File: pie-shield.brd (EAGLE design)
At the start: 160 x 100 mm, 20 parts, among them IC4 NRF24L01SMD, Q2 3.2X2.5CRYSTAL

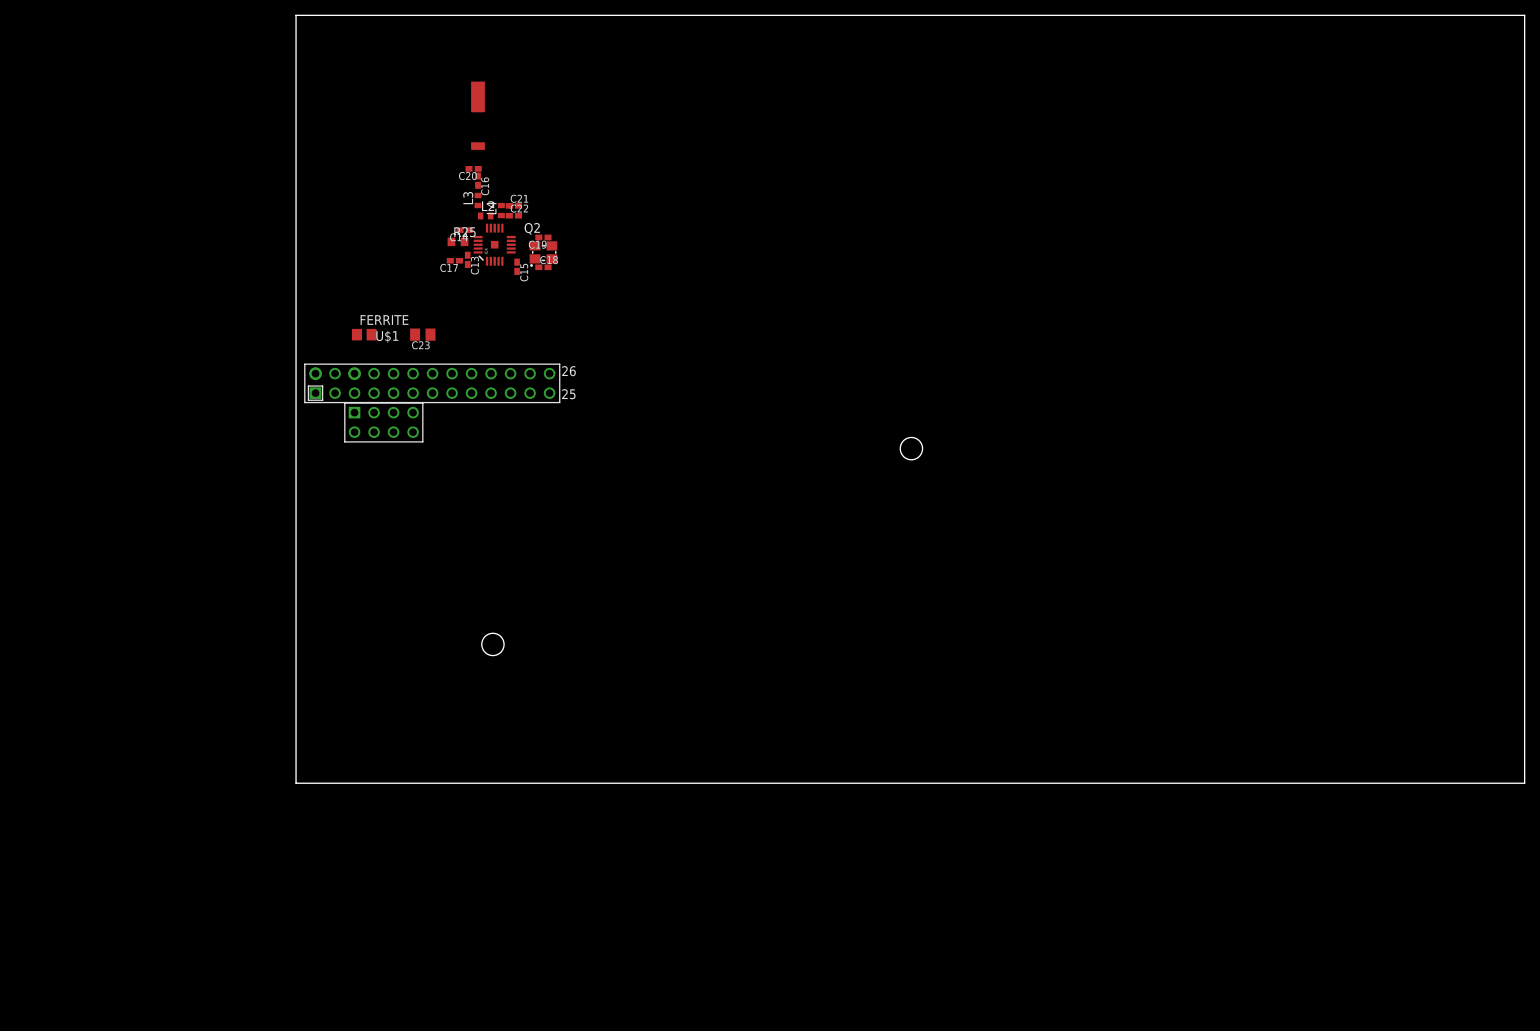
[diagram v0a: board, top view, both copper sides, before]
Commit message: sized board down
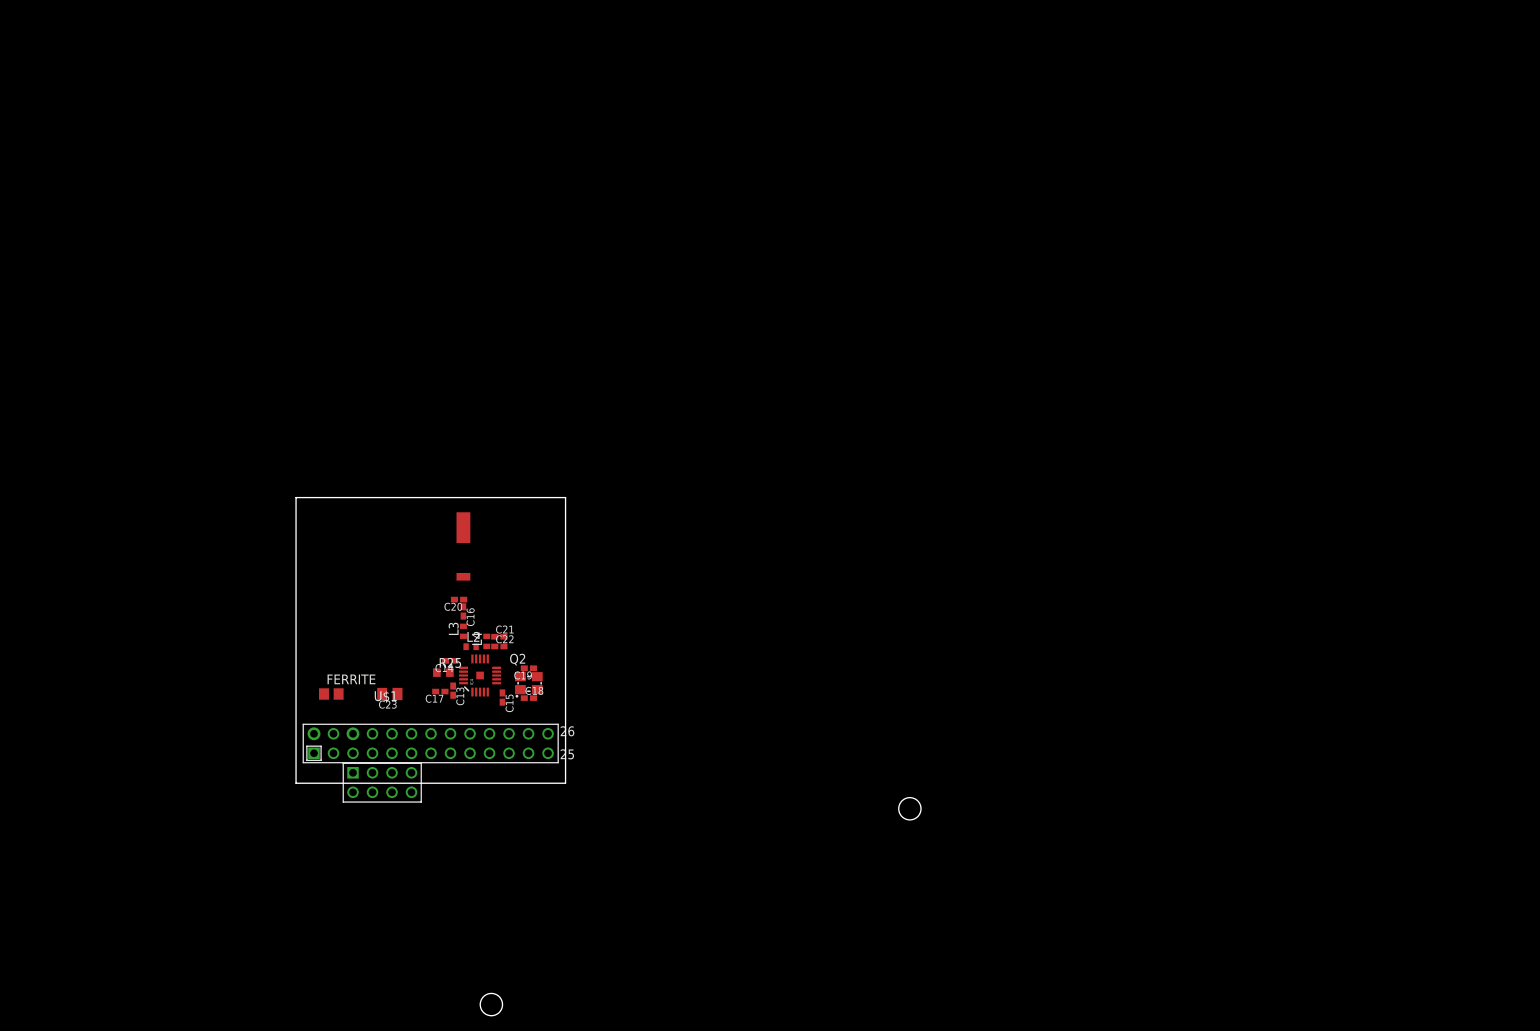
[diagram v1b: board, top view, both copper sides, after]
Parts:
- moved ANT 56.1 mm to (21.8, 29.3)
- moved C15 56.1 mm to (26.9, 11.2)
- moved C17 56.1 mm to (18.8, 11.9)
- moved C20 56.1 mm to (21.2, 23.9)
- moved C21 56.1 mm to (26.5, 19.1)
- moved C14 56.1 mm to (20.1, 15.9)
- moved L3 56.1 mm to (21.8, 19.8)
- moved R25 56.1 mm to (19.2, 14.4)
- moved C13 56.1 mm to (20.5, 12.1)
- moved C16 56.1 mm to (21.8, 22.4)
- moved C18 56.1 mm to (30.3, 11.1)
- moved C19 56.1 mm to (30.3, 15.0)
- moved C22 56.1 mm to (26.5, 17.8)
- moved IC4 56.1 mm to (24.0, 14.0)
- moved L2 56.1 mm to (22.8, 17.8)
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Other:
- board size 160 x 100 mm -> 35.1 x 37.2 mm

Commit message: minisized
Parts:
- moved ANT 15.1 mm to (10.2, 19.7)
- moved C18 13.7 mm to (26.0, 24.1), turned to 90 degrees
- moved Q2 12.7 mm to (24.1, 24.1), turned to 90 degrees
- moved C19 12.3 mm to (22.1, 24.1), turned to 90 degrees
- moved C20 11.3 mm to (12.6, 16.6), turned to 270 degrees
- moved C15 10.1 mm to (25.8, 21.2), turned to 0 degrees
- moved C21 9.47 mm to (17.4, 21.9), turned to 90 degrees
- moved C16 9.23 mm to (14.1, 17.2), turned to 0 degrees
- moved C22 8.78 mm to (18.7, 21.9), turned to 90 degrees
- moved C17 7.99 mm to (26.1, 15.1), turned to 0 degrees
- moved L4 7.03 mm to (18.0, 20.2), turned to 180 degrees
- moved L3 5.69 mm to (16.7, 17.2), turned to 180 degrees
- moved L2 4.09 mm to (18.7, 18.2), turned to 90 degrees
- moved IC4 3.83 mm to (23.1, 17.8), turned to 180 degrees
- moved C13 3.62 mm to (23.8, 13.4)
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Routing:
- net +3V3_RF: track 0.00 -> 47.4 mm, vias 0 -> 3
- net +3V3: track 0.00 -> 7.04 mm
- net N$73: track 0.00 -> 6.46 mm
- net GND: track 0.00 -> 6.17 mm
- net N$11: track 0.00 -> 5.78 mm
- net N$10: track 0.00 -> 4.07 mm
- net N$78: track 0.00 -> 3.84 mm
- net N$79: track 0.00 -> 3.77 mm
- net N$12: track 0.00 -> 3.36 mm
- net N$70: track 0.00 -> 2.82 mm
- net N$71: track 0.00 -> 1.86 mm
- net N$80: track 0.00 -> 1.33 mm
- added copper zone on layer 1, net GND
- added copper zone on layer 16, net GND
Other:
- board size 35.1 x 37.2 mm -> 35.1 x 25.2 mm

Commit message: wired board
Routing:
- net N$10: track 4.07 -> 5.64 mm
- net +3V3_RF: track 47.4 -> 48.4 mm
- net GND: vias 0 -> 43
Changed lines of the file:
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@@
 <contactref element="U$1" pad="P1_9"/>
 <polygon width="0.3048" layer="1" orphans="yes" thermals="no">
-<vertex x="-0.4572" y="13.97"/>
-<vertex x="17.4498" y="14.0208"/>
+<vertex x="-0.7112" y="13.0302"/>
+<vertex x="12.319" y="13.0302"/>
+<vertex x="12.2936" y="15.8496"/>
 <vertex x="21.2852" y="15.6972"/>
-<vertex x="21.3868" y="20.574"/>
-<vertex x="21.336" y="27.7876"/>
+<vertex x="21.3614" y="20.701"/>
+<vertex x="19.5326" y="22.606"/>
+<vertex x="16.0274" y="22.5806"/>
+<vertex x="16.0528" y="27.178"/>
 <vertex x="36.0934" y="27.2034"/>
-<vertex x="35.941" y="-0.9906"/>
-<vertex x="-0.4572" y="-0.3302"/>
+<vertex x="35.7632" y="0.7366"/>
+<vertex x="-0.4064" y="1.016"/>
 </polygon>
 <polygon width="0.3048" layer="16">
-<vertex x="17.3228" y="13.8684"/>
+<vertex x="-0.7112" y="12.954"/>
+<vertex x="12.2936" y="12.954"/>
+<vertex x="12.3444" y="15.9004"/>
 <vertex x="21.2344" y="15.748"/>
-<vertex x="21.2598" y="28.0416"/>
+<vertex x="21.3614" y="20.7772"/>
+<vertex x="19.5072" y="22.5552"/>
+<vertex x="15.9766" y="22.5298"/>
+<vertex x="15.9512" y="27.1018"/>
 <vertex x="35.941" y="27.2034"/>
-<vertex x="35.4584" y="-0.5842"/>
-<vertex x="-0.2286" y="-0.6858"/>
-<vertex x="-0.127" y="13.9192"/>
+<vertex x="35.941" y="1.1176"/>
+<vertex x="-0.5334" y="0.889"/>
 </polygon>
 <wire x1="20.916" y1="17.2508" x2="22.57" y2="17.2508" width="0.3048" layer="1"/>
@@
 <wire x1="23.07" y1="17.7508" x2="23.07" y2="19.9048" width="0.3048" layer="1"/>
 <wire x1="22.57" y1="15.5968" x2="22.57" y2="17.2508" width="0.3048" layer="1"/>
-<wire x1="17.4358" y1="22.4864" x2="18.7058" y2="22.4864" width="0" layer="19" extent="1-1"/>
-<wire x1="22.0792" y1="24.7262" x2="18.7058" y2="22.4864" width="0" layer="19" extent="1-1"/>
-<wire x1="26.02" y1="24.6708" x2="22.0792" y2="24.7262" width="0" layer="19" extent="1-1"/>
-<wire x1="13.21" y1="10.4008" x2="17.58" y2="6.44" width="0" layer="19" extent="1-1"/>
-<wire x1="12.6058" y1="16.0364" x2="13.21" y2="10.4008" width="0" layer="19" extent="1-1"/>
+<via x="31.9024" y="22.3774" extent="1-16" drill="0.5" shape="octagon"/>
+<via x="31.8008" y="18.9738" extent="1-16" drill="0.5" shape="octagon"/>
+<via x="31.877" y="15.8496" extent="1-16" drill="0.5" shape="octagon"/>
+<via x="31.877" y="12.7" extent="1-16" drill="0.5" shape="octagon"/>
+<via x="31.877" y="9.4996" extent="1-16" drill="0.5" shape="octagon"/>
+<via x="1.6256" y="12.573" extent="1-16" drill="0.5" shape="octagon"/>
+<via x="4.3688" y="12.5984" extent="1-16" drill="0.5" shape="octagon"/>
+<via x="7.4422" y="12.5984" extent="1-16" drill="0.5" shape="octagon"/>
+<via x="10.2362" y="12.6746" extent="1-16" drill="0.5" shape="octagon"/>
+<via x="12.827" y="12.7508" extent="1-16" drill="0.5" shape="octagon"/>
+<via x="12.8524" y="14.5542" extent="1-16" drill="0.5" shape="octagon"/>
+<via x="13.9446" y="15.367" extent="1-16" drill="0.5" shape="octagon"/>
+<via x="15.8242" y="15.367" extent="1-16" drill="0.5" shape="octagon"/>
+<via x="19.6088" y="15.367" extent="1-16" drill="0.5" shape="octagon"/>
+<via x="31.8008" y="25.2222" extent="1-16" drill="0.5" shape="octagon"/>
+<via x="16.891" y="25.1714" extent="1-16" drill="0.5" shape="octagon"/>
+<via x="18.9484" y="25.2222" extent="1-16" drill="0.5" shape="octagon"/>
+<via x="20.7772" y="25.3238" extent="1-16" drill="0.5" shape="octagon"/>
+<via x="16.8148" y="23.6982" extent="1-16" drill="0.5" shape="octagon"/>
+<via x="18.9992" y="23.6728" extent="1-16" drill="0.5" shape="octagon"/>
+<via x="20.193" y="22.6314" extent="1-16" drill="0.5" shape="octagon"/>
+<via x="20.6502" y="12.1158" extent="1-16" drill="0.5" shape="octagon"/>
+<via x="20.2184" y="10.0076" extent="1-16" drill="0.5" shape="octagon"/>
+<via x="23.114" y="9.9314" extent="1-16" drill="0.5" shape="octagon"/>
+<via x="24.5364" y="11.8364" extent="1-16" drill="0.5" shape="octagon"/>
+<via x="27.178" y="25.146" extent="1-16" drill="0.5" shape="octagon"/>
+<via x="29.464" y="25.2476" extent="1-16" drill="0.5" shape="octagon"/>
+<via x="21.1836" y="21.5138" extent="1-16" drill="0.5" shape="octagon"/>
+<via x="17.7292" y="15.367" extent="1-16" drill="0.5" shape="octagon"/>
+<via x="1.5494" y="10.7188" extent="1-16" drill="0.5" shape="octagon"/>
+<via x="1.6002" y="9.0424" extent="1-16" drill="0.5" shape="octagon"/>
+<via x="4.9784" y="8.5852" extent="1-16" drill="0.5" shape="octagon"/>
+<via x="7.5692" y="8.636" extent="1-16" drill="0.5" shape="octagon"/>
+<via x="9.7282" y="8.6614" extent="1-16" drill="0.5" shape="octagon"/>
+<via x="11.3284" y="8.1026" extent="1-16" drill="0.5" shape="octagon"/>
+<via x="13.7922" y="7.8232" extent="1-16" drill="0.5" shape="octagon"/>
+<via x="16.383" y="7.8232" extent="1-16" drill="0.5" shape="octagon"/>
+<via x="18.8214" y="7.8232" extent="1-16" drill="0.5" shape="octagon"/>
+<via x="21.4122" y="7.7724" extent="1-16" drill="0.5" shape="octagon"/>
+<via x="23.9014" y="7.7724" extent="1-16" drill="0.5" shape="octagon"/>
+<via x="26.3906" y="7.6708" extent="1-16" drill="0.5" shape="octagon"/>
+<via x="29.0068" y="7.6962" extent="1-16" drill="0.5" shape="octagon"/>
+<via x="31.6484" y="7.5946" extent="1-16" drill="0.5" shape="octagon"/>
 </signal>
 <signal name="+3V3" class="2">
@@
 <wire x1="23.8166" y1="14.0156" x2="23.07" y2="14.7622" width="0.3048" layer="1"/>
 <wire x1="23.07" y1="14.7622" x2="23.07" y2="15.5968" width="0.3048" layer="1"/>
-<wire x1="11.21" y1="10.4008" x2="12.7462" y2="8.8646" width="0.4064" layer="1"/>
-<wire x1="12.7462" y1="8.8646" x2="18.9992" y2="8.8646" width="0.4064" layer="1"/>
-<wire x1="18.9992" y1="8.8646" x2="23.6474" y2="8.8646" width="0.4064" layer="1"/>
-<wire x1="23.6474" y1="8.8646" x2="27.1526" y2="12.3698" width="0.4064" layer="1"/>
 <wire x1="27.1526" y1="19.3054" x2="25.2384" y2="21.2196" width="0.4064" layer="1"/>
 <via x="27.1018" y="19.3294" extent="1-16" drill="0.5" shape="octagon"/>
@@
 <wire x1="20.789" y1="14.4408" x2="19.7494" y2="14.4408" width="0.4064" layer="1"/>
 <wire x1="19.7494" y1="14.4408" x2="19.0246" y2="13.716" width="0.4064" layer="1"/>
-<wire x1="19.0246" y1="13.716" x2="19.0246" y2="8.89" width="0.4064" layer="1"/>
-<wire x1="19.0246" y1="8.89" x2="18.9992" y2="8.8646" width="0.4064" layer="1"/>
+<wire x1="27.1272" y1="12.3952" x2="25.437" y2="12.3952" width="0.3048" layer="1"/>
+<wire x1="25.437" y1="12.3952" x2="23.8166" y2="14.0156" width="0.3048" layer="1"/>
+<wire x1="11.21" y1="10.4008" x2="12.4932" y2="11.684" width="0.4064" layer="1"/>
+<wire x1="12.4932" y1="11.684" x2="18.3134" y2="11.684" width="0.4064" layer="1"/>
+<wire x1="18.3134" y1="11.684" x2="19.7358" y2="11.684" width="0.4064" layer="1"/>
+<wire x1="19.7358" y1="11.684" x2="20.5994" y2="10.8204" width="0.4064" layer="1"/>
+<wire x1="20.5994" y1="10.8204" x2="25.781" y2="10.8204" width="0.4064" layer="1"/>
+<wire x1="25.781" y1="10.8204" x2="27.1272" y2="12.2174" width="0.4064" layer="1"/>
+<wire x1="27.1272" y1="12.2174" x2="27.1272" y2="12.3952" width="0.4064" layer="1"/>
+<wire x1="19.0246" y1="13.716" x2="19.0246" y2="12.3952" width="0.4064" layer="1"/>
+<wire x1="19.0246" y1="12.3952" x2="18.3134" y2="11.684" width="0.4064" layer="1"/>
 <wire x1="27.1526" y1="19.2786" x2="27.1526" y2="19.3054" width="0" layer="19" extent="1-16"/>
-<wire x1="27.1272" y1="12.3952" x2="27.1526" y2="12.3698" width="0" layer="19" extent="16-16"/>
-<wire x1="23.07" y1="14.7622" x2="20.789" y2="14.4408" width="0" layer="19" extent="1-1"/>
+<wire x1="27.1272" y1="12.3952" x2="27.1526" y2="12.3698" width="0" layer="19" extent="1-1"/>
 </signal>
 <signal name="IRQ">
@@
 <wire x1="24.92" y1="23.0008" x2="22.57" y2="20.6508" width="0.3048" layer="1"/>
 <wire x1="22.57" y1="20.6508" x2="22.57" y2="19.9048" width="0.3048" layer="1"/>
-<wire x1="24.92" y1="23.0008" x2="26.02" y2="23.4708" width="0" layer="19" extent="1-1"/>
+<wire x1="26.02" y1="23.4708" x2="24.92" y2="23.4708" width="0.4064" layer="1"/>
+<wire x1="24.92" y1="23.4708" x2="24.92" y2="23.0008" width="0.4064" layer="1"/>
 </signal>
 <signal name="N$11">
@@
 <contactref element="C19" pad="1"/>
 <wire x1="23.22" y1="25.2008" x2="23.22" y2="24.6416" width="0.3048" layer="1"/>
-<wire x1="23.22" y1="24.6416" x2="22.0792" y2="23.5262" width="0.3048" layer="1"/>
+<wire x1="23.22" y1="24.6416" x2="22.0792" y2="23.5262" width="0.4064" layer="1"/>
 <wire x1="22.0792" y1="23.5262" x2="22.0792" y2="19.914" width="0.3048" layer="1"/>
 <wire x1="22.0792" y1="19.914" x2="22.07" y2="19.9048" width="0.3048" layer="1"/>

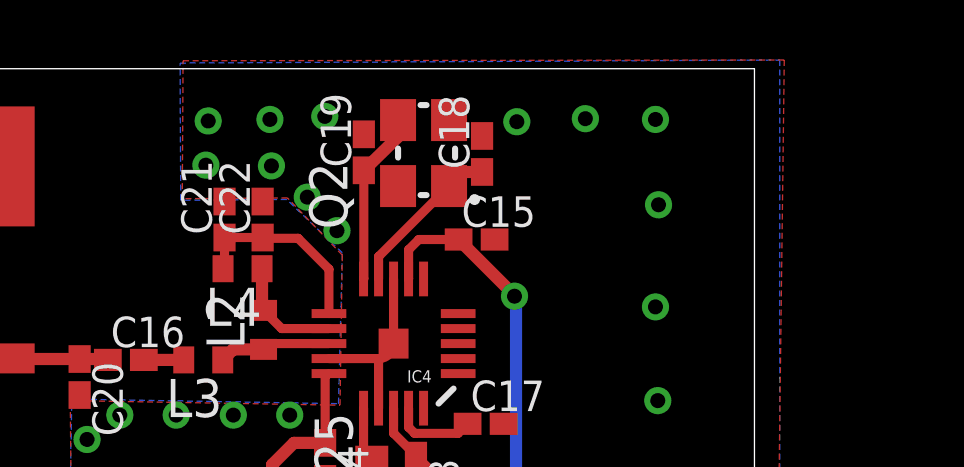
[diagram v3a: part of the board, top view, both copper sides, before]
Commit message: more space for antenna
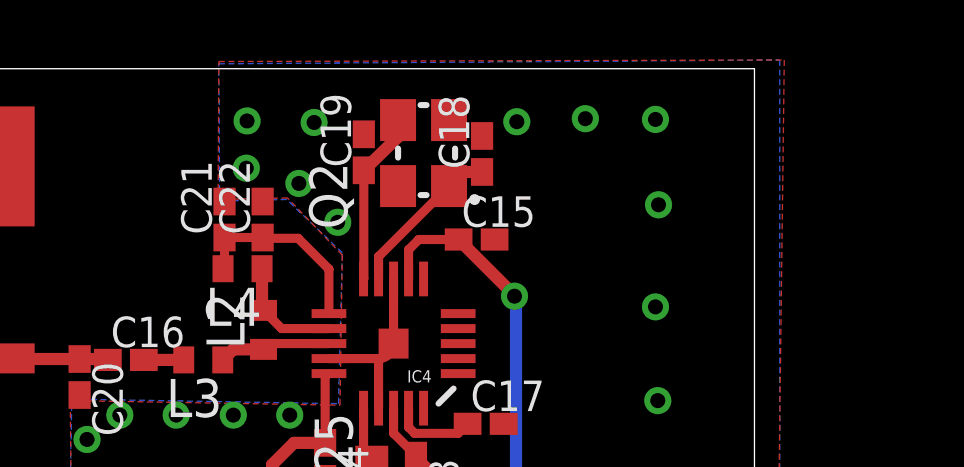
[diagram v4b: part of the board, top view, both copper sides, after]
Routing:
- net GND: vias 43 -> 41
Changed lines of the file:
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@@
 <vertex x="21.3614" y="20.701"/>
 <vertex x="19.5326" y="22.606"/>
-<vertex x="16.0274" y="22.5806"/>
-<vertex x="16.0528" y="27.178"/>
+<vertex x="17.2212" y="22.5552"/>
+<vertex x="17.2466" y="27.1526"/>
 <vertex x="36.0934" y="27.2034"/>
 <vertex x="35.7632" y="0.7366"/>
@@
 <vertex x="21.3614" y="20.7772"/>
 <vertex x="19.5072" y="22.5552"/>
-<vertex x="15.9766" y="22.5298"/>
-<vertex x="15.9512" y="27.1018"/>
+<vertex x="17.272" y="22.5044"/>
+<vertex x="17.2466" y="27.0764"/>
 <vertex x="35.941" y="27.2034"/>
 <vertex x="35.941" y="1.1176"/>
@@
 <via x="19.6088" y="15.367" extent="1-16" drill="0.5" shape="octagon"/>
 <via x="31.8008" y="25.2222" extent="1-16" drill="0.5" shape="octagon"/>
-<via x="16.891" y="25.1714" extent="1-16" drill="0.5" shape="octagon"/>
-<via x="18.9484" y="25.2222" extent="1-16" drill="0.5" shape="octagon"/>
-<via x="20.7772" y="25.3238" extent="1-16" drill="0.5" shape="octagon"/>
-<via x="16.8148" y="23.6982" extent="1-16" drill="0.5" shape="octagon"/>
-<via x="18.9992" y="23.6728" extent="1-16" drill="0.5" shape="octagon"/>
-<via x="20.193" y="22.6314" extent="1-16" drill="0.5" shape="octagon"/>
+<via x="18.1864" y="25.1714" extent="1-16" drill="0.5" shape="octagon"/>
+<via x="20.4216" y="25.1206" extent="1-16" drill="0.5" shape="octagon"/>
+<via x="18.161" y="23.5966" extent="1-16" drill="0.5" shape="octagon"/>
+<via x="19.9136" y="23.0886" extent="1-16" drill="0.5" shape="octagon"/>
 <via x="20.6502" y="12.1158" extent="1-16" drill="0.5" shape="octagon"/>
 <via x="20.2184" y="10.0076" extent="1-16" drill="0.5" shape="octagon"/>
@@
 <via x="27.178" y="25.146" extent="1-16" drill="0.5" shape="octagon"/>
 <via x="29.464" y="25.2476" extent="1-16" drill="0.5" shape="octagon"/>
-<via x="21.1836" y="21.5138" extent="1-16" drill="0.5" shape="octagon"/>
+<via x="21.209" y="21.7932" extent="1-16" drill="0.5" shape="octagon"/>
 <via x="17.7292" y="15.367" extent="1-16" drill="0.5" shape="octagon"/>
 <via x="1.5494" y="10.7188" extent="1-16" drill="0.5" shape="octagon"/>
